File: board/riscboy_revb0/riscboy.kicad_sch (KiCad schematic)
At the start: 104 parts, among them J1 USB_B_Micro, J10 NF, J2 NF, J3 1827928-1 TE, J4 2.54mm, J5 2.54mm, J6 2.54mm, J7 2.54mm, J8 2.5mm-3P-TRS, J9 0.5mm FFC bottom-contact, SW1 membrane, SW10 tactile, SW2 membrane, SW3 membrane, SW4 membrane, SW5 SW_SPDT, SW6 membrane, SW7 membrane, SW8 membrane, SW9 membrane, U1 RP2040, U10 iCE40-HX8k-BG121, U11 W25Q16JV, U2 MIC23050-4YML, U3 W25Q16JV, U4 MCP73831-SOT-23-5, U5 MIC23050-SYML, U6 74LVC2G04, U7 NCP115ASN330, U8 74LVC2G04, U9 CY7C1041CV33, Y1 12M

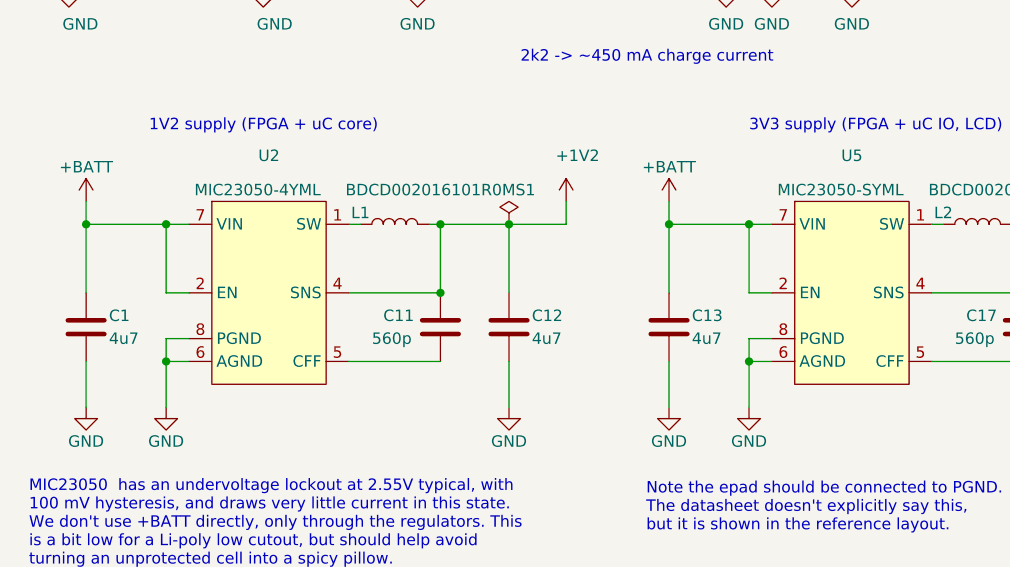
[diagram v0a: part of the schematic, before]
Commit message: Start generating and assigning footprints for rev B board
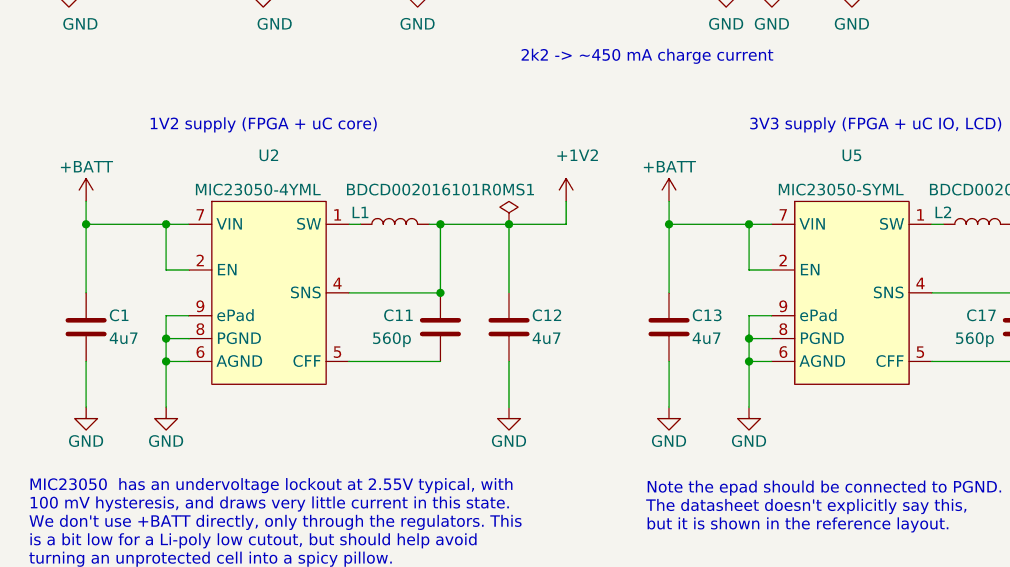
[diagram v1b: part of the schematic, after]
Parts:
- C1, C10, C12, C13, C15, C18, C19, C20, C21, C24, C25, C28, C36, C42, C8: footprint (none) -> riscboy:C_0603_1608Metric_undersilk
- C11, C14, C16, C17, C2, C22, C23, C26, C27, C29, C3, C30, C31, C32, C33, C34, C35, C37, C38, C39, C4, C40, C41, C43, C44, C5, C6, C7, C9: footprint (none) -> riscboy:C_0402_1005Metric_undersilk
- J1: footprint (none) -> Connector_USB:USB_Micro-B_Molex-105017-0001
- J10: footprint (none) -> Connector_PinHeader_2.54mm:PinHeader_2x04_P2.54mm_Vertical
- J2: footprint (none) -> Connector_PinHeader_2.54mm:PinHeader_2x03_P2.54mm_Vertical
- J4: footprint (none) -> Connector_PinHeader_2.54mm:PinHeader_1x03_P2.54mm_Vertical
- J5, J6, J7: footprint (none) -> Connector_PinHeader_2.54mm:PinHeader_1x02_P2.54mm_Vertical
- L1, L2: footprint (none) -> riscboy:L_0806_undersilk
- LS1, R1, R10, R11, R12, R13, R14, R15, R16, R17, R18, R19, R2, R20, R21, R3, R4, R5, R6, R7, R8, R9: footprint (none) -> riscboy:R_0402_1005Metric_undersilk
- R22, SW1, SW2, SW3, SW4, SW6, SW7, SW8, SW9: footprint (none) -> riscboy:membrane-switch-6mm
- U1: footprint (none) -> riscboy:QFN-56_EP_7x7_Pitch0.4mm
- U10: footprint (none) -> riscboy:BGA-121_11x11_9.0x9.0mm
- U11, U3: footprint (none) -> Package_SON:WSON-8-1EP_6x5mm_P1.27mm_EP3.4x4.3mm
- U2, U5: footprint (none) -> riscboy:Micrel_MLF-8-1EP_2x2mm_P0.5mm_EP0.8x1.3mm_ThermalVias
- U4, U7: footprint (none) -> Package_TO_SOT_SMD:SOT-23-5_HandSoldering
- U6, U8: footprint (none) -> Package_TO_SOT_SMD:TSOT-23-6_HandSoldering
- U9: footprint (none) -> riscboy:BGA-48_6x8_6.0x8.0mm
- Y1: footprint (none) -> Crystal:Crystal_SMD_3225-4Pin_3.2x2.5mm
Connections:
- net GND: now also U2.9 (ePad), U5.9 (ePad)

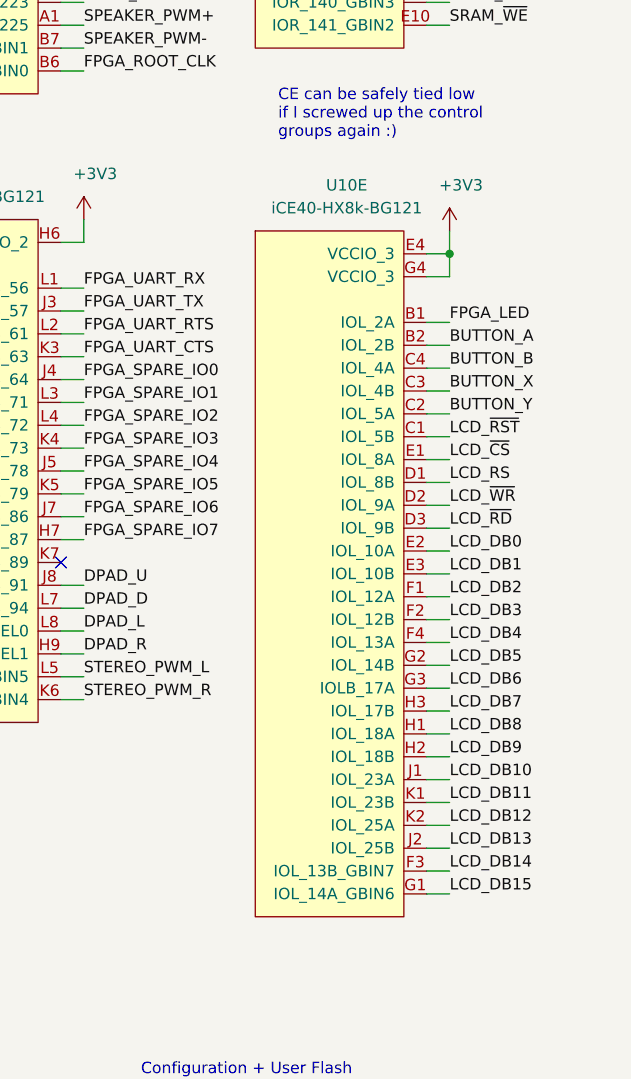
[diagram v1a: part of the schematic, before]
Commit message: Continue with footprint assignment for B0 board
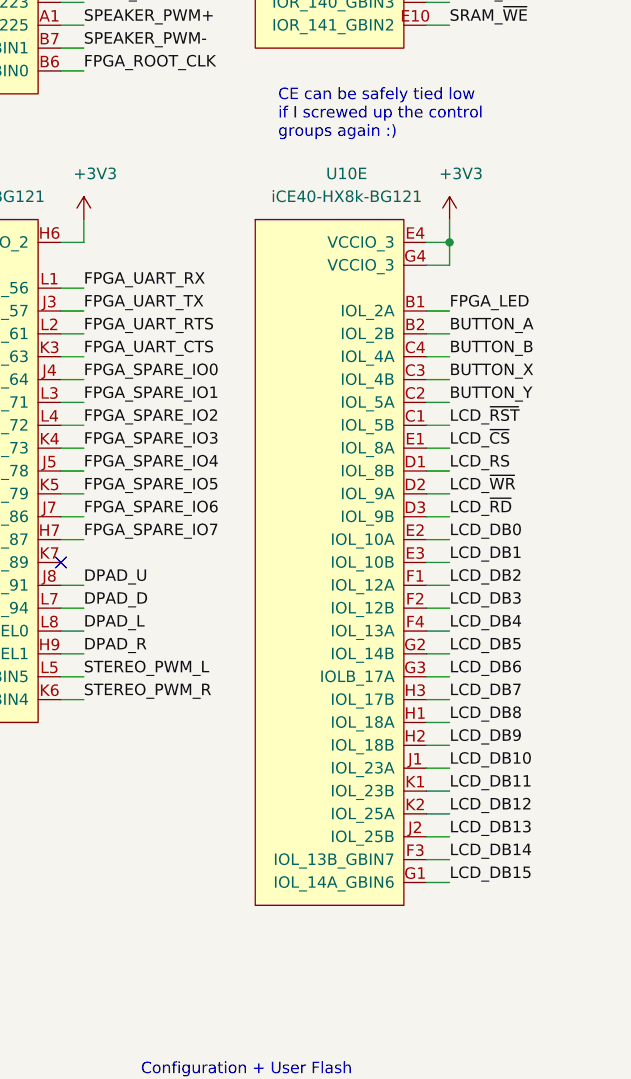
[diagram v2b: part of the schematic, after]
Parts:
- D1: footprint (none) -> riscboy:19-337C-RGB-LED
- J9: footprint (none) -> riscboy:FPC_24_0.5mm
- JP1, JP2: footprint (none) -> riscboy:solderjumper-3-bridged
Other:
- moved on the sheet: U10E

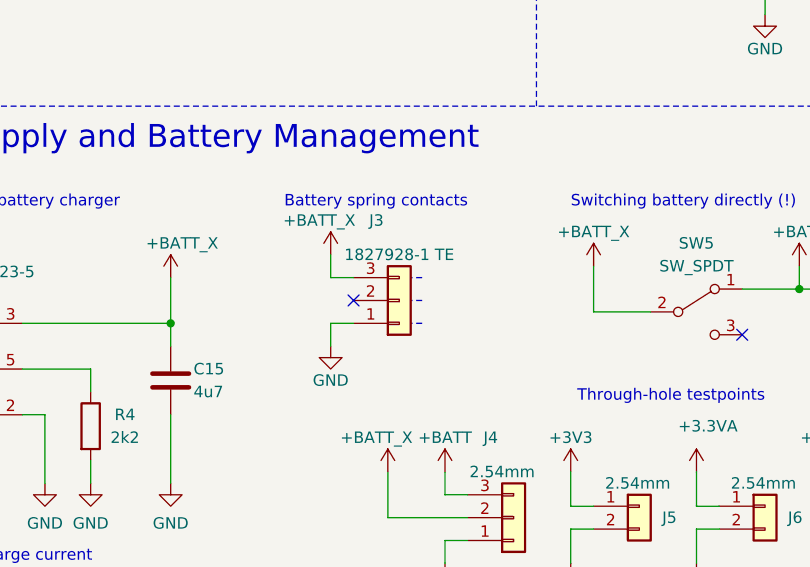
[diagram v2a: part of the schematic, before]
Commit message: Battery footprint for rev b board
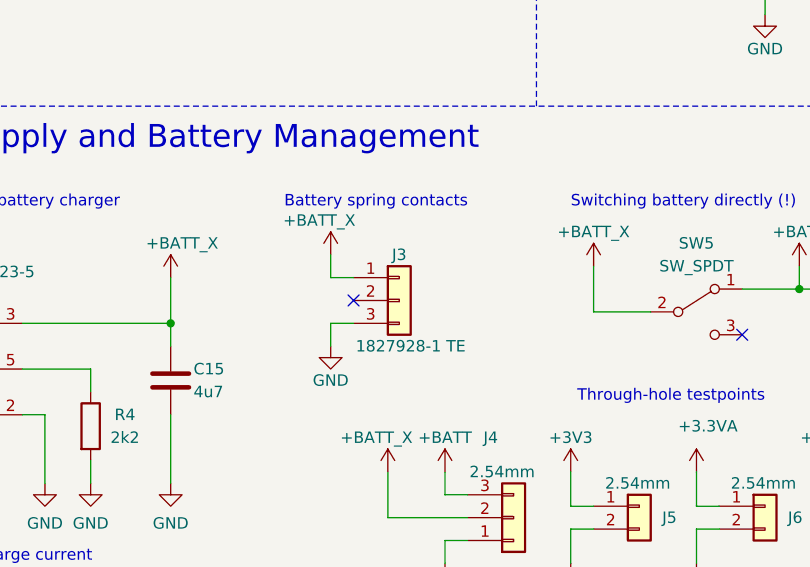
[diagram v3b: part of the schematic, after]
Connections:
- net +BATT_X: now also J3.1 (Pin_1); no longer J3.3 (Pin_3)
- net GND: now also J3.3 (Pin_3); no longer J3.1 (Pin_1)
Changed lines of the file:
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@@
     (stroke (width 0) (type dash) (color 0 0 0 0))
   )
-  (polyline (pts (xy 137.16 195.58) (xy 135.89 195.58))
-    (stroke (width 0) (type dash) (color 0 0 0 0))
-  )
-  (polyline (pts (xy 137.16 198.12) (xy 135.89 198.12))
-    (stroke (width 0) (type dash) (color 0 0 0 0))
-  )
-  (polyline (pts (xy 137.16 200.66) (xy 135.89 200.66))
-    (stroke (width 0) (type dash) (color 0 0 0 0))
-  )
   (polyline (pts (xy 149.86 12.7) (xy 149.86 176.53))
     (stroke (width 0) (type dash) (color 0 0 0 0))
@@
     (pin "2")
   )
-  (symbol (lib_id "Connector_Generic:Conn_01x03") (at 134.62 198.12 0) (mirror x) (unit 1)
+  (symbol (lib_id "Connector_Generic:Conn_01x03") (at 134.62 198.12 0) (unit 1)
     (in_bom yes) (on_board yes)
-    (property "Reference" "J3" (id 0) (at 132.08 189.23 0))
-    (property "Value" "1827928-1 TE" (id 1) (at 134.62 193.04 0))
+    (property "Reference" "J3" (id 0) (at 134.62 193.04 0))
+    (property "Value" "1827928-1 TE" (id 1) (at 135.89 203.2 0))
     (property "Footprint" "" (id 2) (at 134.62 198.12 0)
       (effects (font (size 1.27 1.27)) hide)
@@
     )
     (pin "1")
+    (pin "2")
     (pin "3")
-    (pin "5")
     (pin "4")
-    (pin "2")
+    (pin "5")
     (pin "6")
   )
@@
       (effects (font (size 1.27 1.27)) hide)
     )
-    (pin "4")
     (pin "1")
+    (pin "2")
     (pin "3")
+    (pin "4")
     (pin "5")
-    (pin "2")
   )
   (symbol (lib_id "riscboy:W25Q16JV") (at 68.58 123.19 0) (unit 1)
@@
       (effects (font (size 1.27 1.27)) hide)
     )
-    (pin "8")
-    (pin "4")
-    (pin "6")
     (pin "1")
-    (pin "5")
     (pin "2")
     (pin "3")
+    (pin "4")
+    (pin "5")
+    (pin "6")
     (pin "7")
+    (pin "8")
   )
   (symbol (lib_id "riscboy:W25Q16JV") (at 374.65 218.44 0) (unit 1)
@@
       (effects (font (size 1.27 1.27)) hide)
     )
-    (pin "8")
-    (pin "4")
-    (pin "6")
     (pin "1")
-    (pin "5")
     (pin "2")
     (pin "3")
+    (pin "4")
+    (pin "5")
+    (pin "6")
     (pin "7")
+    (pin "8")
   )
   (symbol (lib_name "riscboy:MIC23050_1") (lib_id "riscboy:MIC23050") (at 44.45 252.73 0) (unit 1)
@@
       (effects (font (size 1.27 1.27)) hide)
     )
-    (pin "7")
-    (pin "2")
-    (pin "8")
-    (pin "6")
     (pin "1")
+    (pin "2")
     (pin "4")
     (pin "5")
+    (pin "6")
+    (pin "7")
+    (pin "8")
     (pin "9")
   )
@@
       (effects (font (size 1.27 1.27)) hide)
     )
-    (pin "7")
-    (pin "2")
-    (pin "8")
-    (pin "6")
     (pin "1")
+    (pin "2")
     (pin "4")
     (pin "5")
+    (pin "6")
+    (pin "7")
+    (pin "8")
     (pin "9")
   )
@@
       (effects (font (size 1.27 1.27)) hide)
     )
+    (pin "A1")
+    (pin "A2")
     (pin "A3")
     (pin "A4")
     (pin "A5")
+    (pin "B1")
+    (pin "B2")
     (pin "B3")
     (pin "B4")
+    (pin "B5")
+    (pin "B6")
+    (pin "C1")
+    (pin "C2")
     (pin "C3")
     (pin "C4")
-    (pin "D4")
-    (pin "H2")
-    (pin "H3")
-    (pin "H4")
-    (pin "H5")
-    (pin "G3")
-    (pin "G4")
-    (pin "F3")
-    (pin "F4")
-    (pin "E4")
-    (pin "D3")
-    (pin "B6")
     (pin "C5")
     (pin "C6")
+    (pin "D1")
+    (pin "D2")
+    (pin "D3")
+    (pin "D4")
     (pin "D5")
+    (pin "D6")
+    (pin "E1")
+    (pin "E2")
+    (pin "E4")
     (pin "E5")
+    (pin "E6")
+    (pin "F1")
+    (pin "F2")
+    (pin "F3")
+    (pin "F4")
     (pin "F5")
     (pin "F6")
-    (pin "G6")
-    (pin "B1")
-    (pin "C1")
-    (pin "C2")
-    (pin "D2")
-    (pin "E2")
-    (pin "F2")
-    (pin "F1")
     (pin "G1")
-    (pin "B2")
-    (pin "A1")
-    (pin "A2")
-    (pin "B5")
+    (pin "G3")
+    (pin "G4")
     (pin "G5")
-    (pin "E1")
-    (pin "D6")
-    (pin "E6")
-    (pin "D1")
+    (pin "G6")
+    (pin "H2")
+    (pin "H3")
+    (pin "H4")
+    (pin "H5")
   )
   (symbol (lib_id "riscboy:iCE40-HX8k-BG121") (at 335.28 35.56 0) (unit 2)

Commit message: Create TRS footprint, assign tact switch footprint
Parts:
- J3: footprint (none) -> riscboy:1827928-1-battery
- J8: footprint (none) -> riscboy:SJ-2523-SMT-TRS
- SW10: footprint (none) -> Button_Switch_SMD:SW_Push_1P1T_NO_6x6mm_H9.5mm
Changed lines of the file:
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@@
     (property "Reference" "SW10" (id 0) (at 224.79 158.75 0))
     (property "Value" "tactile" (id 1) (at 220.98 163.83 0))
-    (property "Footprint" "" (id 2) (at 220.98 156.21 0)
+    (property "Footprint" "Button_Switch_SMD:SW_Push_1P1T_NO_6x6mm_H9.5mm" (id 2) (at 220.98 156.21 0)
       (effects (font (size 1.27 1.27)) hide)
     )
@@
     (property "Reference" "J3" (id 0) (at 134.62 193.04 0))
     (property "Value" "1827928-1 TE" (id 1) (at 135.89 203.2 0))
-    (property "Footprint" "" (id 2) (at 134.62 198.12 0)
+    (property "Footprint" "riscboy:1827928-1-battery" (id 2) (at 134.62 198.12 0)
       (effects (font (size 1.27 1.27)) hide)
     )
@@
       (effects (font (size 1.27 1.27)) (justify right))
     )
-    (property "Footprint" "" (id 2) (at 256.54 40.64 0)
+    (property "Footprint" "riscboy:SJ-2523-SMT-TRS" (id 2) (at 256.54 40.64 0)
       (effects (font (size 1.27 1.27)) hide)
     )
@@
     )
     (path "/3630d1ab-0593-46d6-85e2-28d8b5df0385"
-      (reference "J3") (unit 1) (value "1827928-1 TE") (footprint "")
+      (reference "J3") (unit 1) (value "1827928-1 TE") (footprint "riscboy:1827928-1-battery")
     )
     (path "/1fe9d450-9762-4051-83c2-d081c2ee1598"
@@
     )
     (path "/695285e8-768f-4e6e-85a7-b4ddddfd30dc"
-      (reference "J8") (unit 1) (value "2.5mm-3P-TRS") (footprint "")
+      (reference "J8") (unit 1) (value "2.5mm-3P-TRS") (footprint "riscboy:SJ-2523-SMT-TRS")
     )
     (path "/50060aee-ba17-41fe-a373-ea0d5a28e839"
@@
     )
     (path "/8e283e12-0bfd-487d-9df0-20b5b1d55611"
-      (reference "SW10") (unit 1) (value "tactile") (footprint "")
+      (reference "SW10") (unit 1) (value "tactile") (footprint "Button_Switch_SMD:SW_Push_1P1T_NO_6x6mm_H9.5mm")
     )
     (path "/6be811df-edd7-4694-bd9b-da439be69642"

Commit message: Select a close-enough SPDT switch. Finished with footprints!
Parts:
- SW5: footprint (none) -> riscboy:CSS-1210B-SPDT
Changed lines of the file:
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@@
     (pin "3")
   )
-  (symbol (lib_name "riscboy:74LVC2G04_5") (lib_id "riscboy:74LVC2G04") (at 173.99 38.1 0) (mirror y) (unit 3)
+  (symbol (lib_id "riscboy:74LVC2G04") (at 173.99 38.1 0) (mirror y) (unit 3)
     (in_bom yes) (on_board yes)
     (property "Reference" "U6" (id 0) (at 177.8 38.1 0)
@@
     (pin "5")
   )
-  (symbol (lib_name "riscboy:74LVC2G04_1") (lib_id "riscboy:74LVC2G04") (at 231.14 90.17 0) (mirror y) (unit 3)
+  (symbol (lib_id "riscboy:74LVC2G04") (at 231.14 90.17 0) (mirror y) (unit 3)
     (in_bom yes) (on_board yes)
     (property "Reference" "U8" (id 0) (at 234.95 90.17 0)
@@
     (property "Reference" "SW5" (id 0) (at 167.64 191.77 0))
     (property "Value" "SW_SPDT" (id 1) (at 167.64 194.31 0))
-    (property "Footprint" "" (id 2) (at 167.64 199.39 0)
+    (property "Footprint" "riscboy:CSS-1210B-SPDT" (id 2) (at 167.64 199.39 0)
       (effects (font (size 1.27 1.27)) hide)
     )
@@
     (pin "T")
   )
-  (symbol (lib_name "riscboy:74LVC2G04_3") (lib_id "riscboy:74LVC2G04") (at 177.8 27.94 0) (unit 1)
+  (symbol (lib_id "riscboy:74LVC2G04") (at 177.8 27.94 0) (unit 1)
     (in_bom yes) (on_board yes)
     (property "Reference" "U6" (id 0) (at 179.07 20.32 0))
@@
     (pin "6")
   )
-  (symbol (lib_name "riscboy:74LVC2G04_4") (lib_id "riscboy:74LVC2G04") (at 177.8 50.8 0) (unit 2)
+  (symbol (lib_id "riscboy:74LVC2G04") (at 177.8 50.8 0) (unit 2)
     (in_bom yes) (on_board yes)
     (property "Reference" "U6" (id 0) (at 179.07 46.99 0))
@@
     (pin "6")
   )
-  (symbol (lib_name "riscboy:74LVC2G04_2") (lib_id "riscboy:74LVC2G04") (at 177.8 95.25 0) (unit 2)
+  (symbol (lib_id "riscboy:74LVC2G04") (at 177.8 95.25 0) (unit 2)
     (in_bom yes) (on_board yes)
     (property "Reference" "U8" (id 0) (at 179.07 91.44 0))
@@
     (pin "8")
   )
-  (symbol (lib_name "riscboy:MIC23050_1") (lib_id "riscboy:MIC23050") (at 44.45 252.73 0) (unit 1)
+  (symbol (lib_id "riscboy:MIC23050") (at 44.45 252.73 0) (unit 1)
     (in_bom yes) (on_board yes)
     (property "Reference" "U2" (id 0) (at 44.45 237.49 0))
@@
     (pin "L6")
   )
-  (symbol (lib_name "riscboy:RP2040_1") (lib_id "riscboy:RP2040") (at 110.49 27.94 0) (unit 3)
+  (symbol (lib_id "riscboy:RP2040") (at 110.49 27.94 0) (unit 3)
     (in_bom yes) (on_board yes)
     (property "Reference" "U1" (id 0) (at 113.03 22.86 0))
@@
     (pin "56")
   )
-  (symbol (lib_name "riscboy:RP2040_2") (lib_id "riscboy:RP2040") (at 34.29 29.21 0) (unit 1)
+  (symbol (lib_id "riscboy:RP2040") (at 34.29 29.21 0) (unit 1)
     (in_bom yes) (on_board yes)
     (property "Reference" "U1" (id 0) (at 36.83 24.13 0))
@@
     )
     (path "/67f57f66-3378-4168-8ac8-8fa8cb449b09"
-      (reference "SW5") (unit 1) (value "SW_SPDT") (footprint "")
+      (reference "SW5") (unit 1) (value "SW_SPDT") (footprint "riscboy:CSS-1210B-SPDT")
     )
     (path "/e7ffe1ac-7867-4d27-b4fe-60f9ea778787"
